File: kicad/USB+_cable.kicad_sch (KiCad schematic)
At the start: 5 parts, among them J1401 USB_C_Receptacle, J1402 USB_C_Receptacle

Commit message: Updated Digikey part numbers
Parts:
- J1402: Digikey WM12856CT-ND -> 664-12402072E512ACT-ND
- R1401: Digikey (none) -> P330JCT-ND; Purpose (none) -> LED current limiter
- R1402: Digikey (none) -> P1.0KJCT-ND; Purpose (none) -> LED current limiter
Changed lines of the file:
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@@
       (effects (font (size 1.524 1.524)) hide)
+    )
+    (property "Digikey" "P330JCT-ND" (id 4) (at 119.38 142.24 0)
+      (effects (font (size 1.27 1.27)) hide)
+    )
+    (property "Purpose" "LED current limiter" (id 5) (at 119.38 142.24 0)
+      (effects (font (size 1.27 1.27)) hide)
     )
     (pin "1")
@@
       (effects (font (size 1.27 1.27)) hide)
     )
-    (property "Digikey" "WM12856CT-ND" (id 5) (at 213.36 88.9 0)
+    (property "Digikey" "664-12402072E512ACT-ND" (id 5) (at 213.36 88.9 0)
       (effects (font (size 1.27 1.27)) hide)
     )
@@
       (effects (font (size 1.524 1.524)) hide)
     )
+    (property "Digikey" "P1.0KJCT-ND" (id 4) (at 134.62 142.24 0)
+      (effects (font (size 1.27 1.27)) hide)
+    )
+    (property "Purpose" "LED current limiter" (id 5) (at 134.62 142.24 0)
+      (effects (font (size 1.27 1.27)) hide)
+    )
     (pin "1")

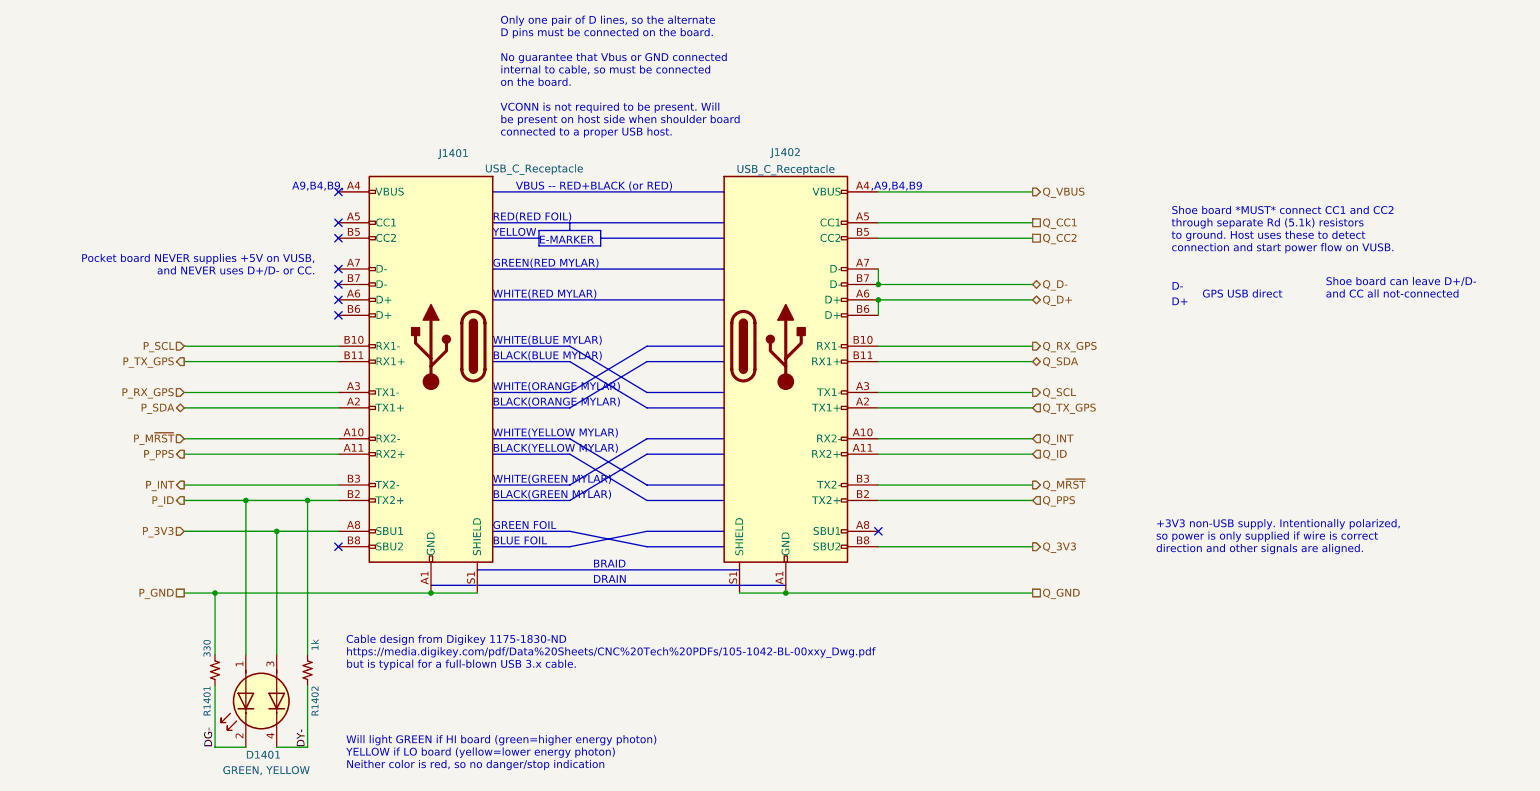
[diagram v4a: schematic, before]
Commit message: Added reference to USB cable on BOM
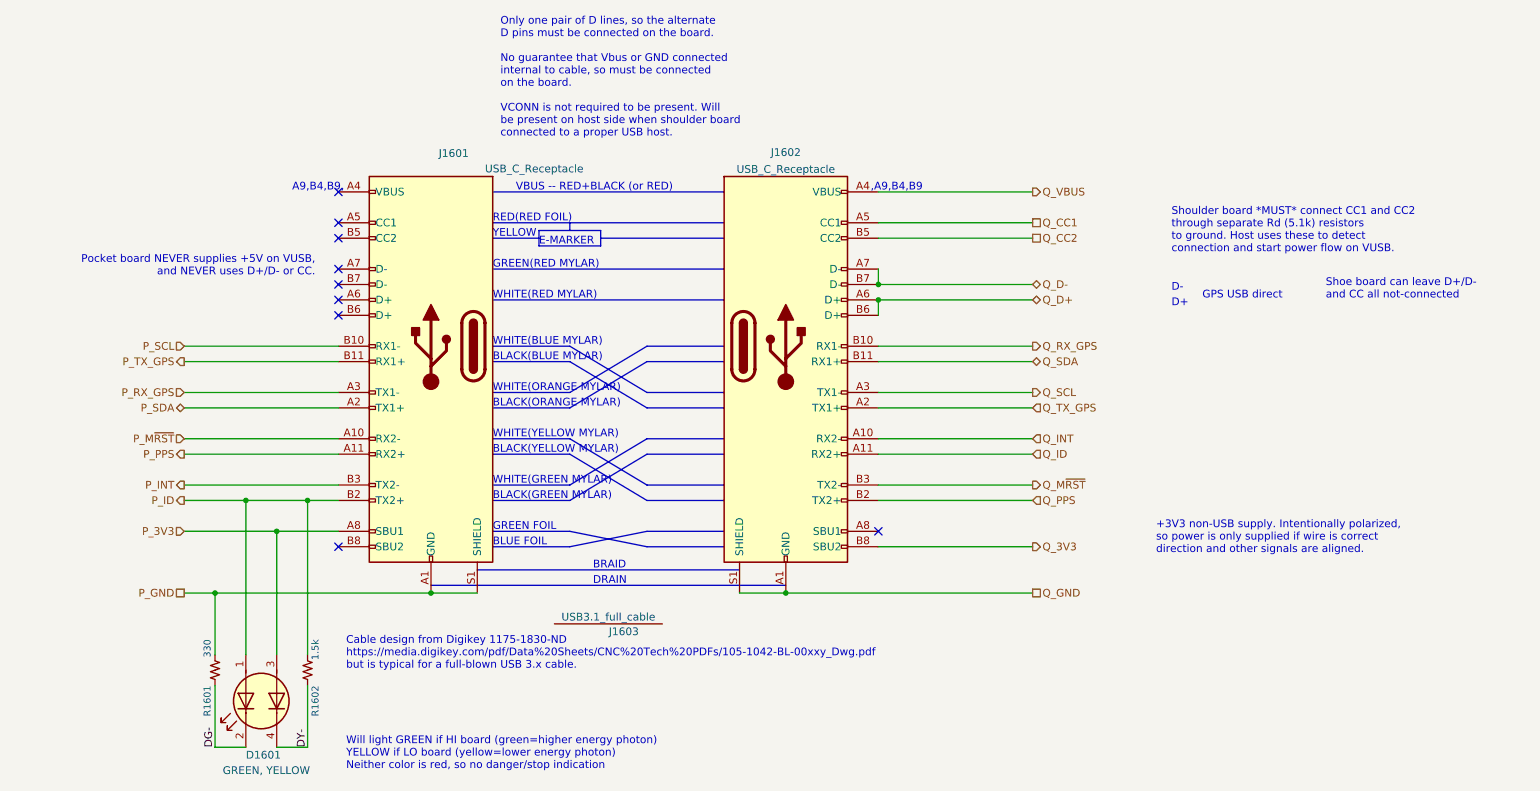
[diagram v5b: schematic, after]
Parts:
- added J1603: USB3.1_full_cable, symbol KwanSystems:USB3.1_full_cable
- R1602: renamed from R1402; value 1k -> 1.5k
- renumbered D1401 to D1601, J1401 to J1601, J1402 to J1602, R1401 to R1601
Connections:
- net at J1601.A4 (VBUS): now also J1601.A9 (VBUS), J1601.B4 (VBUS), J1601.B9 (VBUS)
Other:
- note added: "Shoulder board *MUST* connect CC1 and CC2 through separate Rd (5.1k) resistors to ground. Host uses these to detect connection and start power flow on VUSB."
- note removed: "Shoe board *MUST* connect CC1 and CC2 through separate Rd (5.1k) resistors to ground. Host uses these to detect connection and start power flow on VUSB."
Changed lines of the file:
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@@
     (effects (font (size 1.27 1.27)) (justify left bottom))
   )
-  (text "Shoe board *MUST* connect CC1 and CC2\nthrough separate Rd (5.1k) resistors \nto ground. Host uses these to detect\nconnection and start power flow on VUSB."
+  (text "Shoulder board *MUST* connect CC1 and CC2\nthrough separate Rd (5.1k) resistors \nto ground. Host uses these to detect\nconnection and start power flow on VUSB."
     (at 276.86 73.66 0)
     (effects (font (size 1.27 1.27)) (justify left bottom))
@@
     (effects (font (size 1.27 1.27)) (justify right))
   )
-  (symbol (lib_name "USB_C_Receptacle_1") (lib_id "Connector:USB_C_Receptacle") (at 154.94 88.9 0) (mirror y)
+  (symbol (lib_id "Connector:USB_C_Receptacle") (at 154.94 88.9 0) (mirror y)
     (in_bom yes) (on_board yes)
-    (property "Reference" "J1401" (id 0) (at 156.21 57.15 0)
+    (property "Reference" "J1601" (id 0) (at 156.21 57.15 0)
       (effects (font (size 1.27 1.27)) (justify right))
     )
@@
     )
     (property "Digikey" "664-12402072E512ACT-ND" (id 5) (at 154.94 88.9 0)
-      (effects (font (size 1.27 1.27)) hide)
-    )
-    (pin "A1")
-    (pin "A10")
-    (pin "A11")
-    (pin "A12")
-    (pin "A2")
-    (pin "A3")
-    (pin "A4")
-    (pin "A5")
-    (pin "A6")
-    (pin "A7")
-    (pin "A8")
-    (pin "B1")
-    (pin "B10")
-    (pin "B11")
-    (pin "B12")
-    (pin "B2")
-    (pin "B3")
-    (pin "B5")
-    (pin "B6")
-    (pin "B7")
-    (pin "B8")
-    (pin "S1")
-  )
-  (symbol (lib_id "Device:LED_Dual_AKAK") (at 127 147.32 90) (mirror x)
-    (in_bom yes) (on_board yes)
-    (property "Reference" "D1401" (id 0) (at 124.46 156.21 90)
-      (effects (font (size 1.27 1.27)) (justify right))
-    )
-    (property "Value" "GREEN, YELLOW" (id 1) (at 120.65 158.75 90)
-      (effects (font (size 1.27 1.27)) (justify right))
-    )
-    (property "Footprint" "KwanSystems:LEDKingbrightAPHB" (id 2) (at 127 148.082 0)
-      (effects (font (size 1.27 1.27)) hide)
-    )
-    (property "Datasheet" "~" (id 3) (at 127 148.082 0)
-      (effects (font (size 1.27 1.27)) hide)
-    )
-    (property "Digikey" "754-1956-1-ND" (id 4) (at 127 147.32 0)
-      (effects (font (size 1.27 1.27)) hide)
-    )
-    (property "Purpose" "Remote ID indicator" (id 5) (at 127 147.32 0)
-      (effects (font (size 1.27 1.27)) hide)
-    )
-    (pin "1")
-    (pin "2")
-    (pin "3")
-    (pin "4")
-  )
-  (symbol (lib_id "KwanSystems:RESISTOR") (at 119.38 142.24 90)
-    (in_bom yes) (on_board yes)
-    (property "Reference" "R1401" (id 0) (at 118.11 144.78 0)
-      (effects (font (size 1.143 1.143)) (justify right))
-    )
-    (property "Value" "330" (id 1) (at 118.11 137.16 0)
-      (effects (font (size 1.143 1.143)) (justify right))
-    )
-    (property "Footprint" "Resistor_SMD:R_0402_1005Metric" (id 2) (at 115.57 140.843 0)
-      (effects (font (size 0.508 0.508)) hide)
-    )
-    (property "Datasheet" "" (id 3) (at 127 131.445 0)
-      (effects (font (size 1.524 1.524)) hide)
-    )
-    (property "Digikey" "P330JCT-ND" (id 4) (at 119.38 142.24 0)
-      (effects (font (size 1.27 1.27)) hide)
-    )
-    (property "Purpose" "LED current limiter" (id 5) (at 119.38 142.24 0)
-      (effects (font (size 1.27 1.27)) hide)
-    )
-    (pin "1")
-    (pin "2")
-  )
-  (symbol (lib_id "Connector:USB_C_Receptacle") (at 213.36 88.9 0)
-    (in_bom yes) (on_board yes) (fields_autoplaced)
-    (property "Reference" "J1402" (id 0) (at 213.36 56.9935 0))
-    (property "Value" "USB_C_Receptacle" (id 1) (at 213.36 59.7686 0))
-    (property "Footprint" "KwanSystems:USB_C_Amphenol_MidMount" (id 2) (at 217.17 88.9 0)
-      (effects (font (size 1.27 1.27)) hide)
-    )
-    (property "Datasheet" "https://www.usb.org/sites/default/files/documents/usb_type-c.zip" (id 3) (at 217.17 88.9 0)
-      (effects (font (size 1.27 1.27)) hide)
-    )
-    (property "Purpose" "Remote board USB+ connector" (id 4) (at 213.36 88.9 0)
-      (effects (font (size 1.27 1.27)) hide)
-    )
-    (property "Digikey" "664-12402072E512ACT-ND" (id 5) (at 213.36 88.9 0)
       (effects (font (size 1.27 1.27)) hide)
     )
@@
     (pin "S1")
   )
+  (symbol (lib_id "Device:LED_Dual_AKAK") (at 127 147.32 90) (mirror x)
+    (in_bom yes) (on_board yes)
+    (property "Reference" "D1601" (id 0) (at 124.46 156.21 90)
+      (effects (font (size 1.27 1.27)) (justify right))
+    )
+    (property "Value" "GREEN, YELLOW" (id 1) (at 120.65 158.75 90)
+      (effects (font (size 1.27 1.27)) (justify right))
+    )
+    (property "Footprint" "KwanSystems:LEDKingbrightAPHB" (id 2) (at 127 148.082 0)
+      (effects (font (size 1.27 1.27)) hide)
+    )
+    (property "Datasheet" "~" (id 3) (at 127 148.082 0)
+      (effects (font (size 1.27 1.27)) hide)
+    )
+    (property "Digikey" "754-1956-1-ND" (id 4) (at 127 147.32 0)
+      (effects (font (size 1.27 1.27)) hide)
+    )
+    (property "Purpose" "Remote ID indicator" (id 5) (at 127 147.32 0)
+      (effects (font (size 1.27 1.27)) hide)
+    )
+    (pin "1")
+    (pin "2")
+    (pin "3")
+    (pin "4")
+  )
+  (symbol (lib_id "KwanSystems:RESISTOR") (at 119.38 142.24 90)
+    (in_bom yes) (on_board yes)
+    (property "Reference" "R1601" (id 0) (at 118.11 144.78 0)
+      (effects (font (size 1.143 1.143)) (justify right))
+    )
+    (property "Value" "330" (id 1) (at 118.11 137.16 0)
+      (effects (font (size 1.143 1.143)) (justify right))
+    )
+    (property "Footprint" "Resistor_SMD:R_0402_1005Metric" (id 2) (at 115.57 140.843 0)
+      (effects (font (size 0.508 0.508)) hide)
+    )
+    (property "Datasheet" "" (id 3) (at 127 131.445 0)
+      (effects (font (size 1.524 1.524)) hide)
+    )
+    (property "Digikey" "P330JCT-ND" (id 4) (at 119.38 142.24 0)
+      (effects (font (size 1.27 1.27)) hide)
+    )
+    (property "Purpose" "LED current limiter" (id 5) (at 119.38 142.24 0)
+      (effects (font (size 1.27 1.27)) hide)
+    )
+    (pin "1")
+    (pin "2")
+  )
+  (symbol (lib_id "Connector:USB_C_Receptacle") (at 213.36 88.9 0)
+    (in_bom yes) (on_board yes) (fields_autoplaced)
+    (property "Reference" "J1602" (id 0) (at 213.36 56.9935 0))
+    (property "Value" "USB_C_Receptacle" (id 1) (at 213.36 59.7686 0))
+    (property "Footprint" "KwanSystems:USB_C_Amphenol_MidMount" (id 2) (at 217.17 88.9 0)
+      (effects (font (size 1.27 1.27)) hide)
+    )
+    (property "Datasheet" "https://www.usb.org/sites/default/files/documents/usb_type-c.zip" (id 3) (at 217.17 88.9 0)
+      (effects (font (size 1.27 1.27)) hide)
+    )
+    (property "Purpose" "Remote board USB+ connector" (id 4) (at 213.36 88.9 0)
+      (effects (font (size 1.27 1.27)) hide)
+    )
+    (property "Digikey" "664-12402072E512ACT-ND" (id 5) (at 213.36 88.9 0)
+      (effects (font (size 1.27 1.27)) hide)
+    )
+    (pin "A1")
+    (pin "A10")
+    (pin "A11")
+    (pin "A12")
+    (pin "A2")
+    (pin "A3")
+    (pin "A4")
+    (pin "A5")
+    (pin "A6")
+    (pin "A7")
+    (pin "A8")
+    (pin "A9")
+    (pin "B1")
+    (pin "B10")
+    (pin "B11")
+    (pin "B12")
+    (pin "B2")
+    (pin "B3")
+    (pin "B4")
+    (pin "B5")
+    (pin "B6")
+    (pin "B7")
+    (pin "B8")
+    (pin "B9")
+    (pin "S1")
+  )
+  (symbol (lib_id "KwanSystems:USB3.1_full_cable") (at 184.15 133.35 0)
+    (in_bom yes) (on_board no)
+    (property "Reference" "J1603" (id 0) (at 186.69 135.89 0))
+    (property "Value" "USB3.1_full_cable" (id 1) (at 184.15 133.4794 0))
+    (property "Footprint" "" (id 2) (at 184.15 133.35 0)
+      (effects (font (size 1.27 1.27)) hide)
+    )
+    (property "Datasheet" "" (id 3) (at 184.15 133.35 0)
+      (effects (font (size 1.27 1.27)) hide)
+    )
+    (property "Digikey" "839-10-03674-ND" (id 4) (at 184.15 133.35 0)
+      (effects (font (size 1.27 1.27)) hide)
+    )
+    (property "Purpose" "Connector cables" (id 5) (at 184.15 133.35 0)
+      (effects (font (size 1.27 1.27)) hide)
+    )
+  )
   (symbol (lib_id "KwanSystems:RESISTOR") (at 134.62 142.24 90)
     (in_bom yes) (on_board yes)
-    (property "Reference" "R1402" (id 0) (at 135.89 144.78 0)
+    (property "Reference" "R1602" (id 0) (at 135.89 144.78 0)
       (effects (font (size 1.143 1.143)) (justify right))
     )
-    (property "Value" "1k" (id 1) (at 135.89 137.16 0)
+    (property "Value" "1.5k" (id 1) (at 135.89 137.16 0)
       (effects (font (size 1.143 1.143)) (justify right))
     )

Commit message: Added a NC to the board
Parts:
- renumbered D1601 to D1401, J1601 to J1401, J1602 to J1402, J1603 to J1403, R1601 to R1401, R1602 to R1402
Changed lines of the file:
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@@
   (symbol (lib_id "Connector:USB_C_Receptacle") (at 154.94 88.9 0) (mirror y)
     (in_bom yes) (on_board yes)
-    (property "Reference" "J1601" (id 0) (at 156.21 57.15 0)
+    (property "Reference" "J1401" (id 0) (at 156.21 57.15 0)
       (effects (font (size 1.27 1.27)) (justify right))
     )
@@
   (symbol (lib_id "Device:LED_Dual_AKAK") (at 127 147.32 90) (mirror x)
     (in_bom yes) (on_board yes)
-    (property "Reference" "D1601" (id 0) (at 124.46 156.21 90)
+    (property "Reference" "D1401" (id 0) (at 124.46 156.21 90)
       (effects (font (size 1.27 1.27)) (justify right))
     )
@@
   (symbol (lib_id "KwanSystems:RESISTOR") (at 119.38 142.24 90)
     (in_bom yes) (on_board yes)
-    (property "Reference" "R1601" (id 0) (at 118.11 144.78 0)
+    (property "Reference" "R1401" (id 0) (at 118.11 144.78 0)
       (effects (font (size 1.143 1.143)) (justify right))
     )
@@
   (symbol (lib_id "Connector:USB_C_Receptacle") (at 213.36 88.9 0)
     (in_bom yes) (on_board yes) (fields_autoplaced)
-    (property "Reference" "J1602" (id 0) (at 213.36 56.9935 0))
+    (property "Reference" "J1402" (id 0) (at 213.36 56.9935 0))
     (property "Value" "USB_C_Receptacle" (id 1) (at 213.36 59.7686 0))
     (property "Footprint" "KwanSystems:USB_C_Amphenol_MidMount" (id 2) (at 217.17 88.9 0)
@@
   (symbol (lib_id "KwanSystems:USB3.1_full_cable") (at 184.15 133.35 0)
     (in_bom yes) (on_board no)
-    (property "Reference" "J1603" (id 0) (at 186.69 135.89 0))
+    (property "Reference" "J1403" (id 0) (at 186.69 135.89 0))
     (property "Value" "USB3.1_full_cable" (id 1) (at 184.15 133.4794 0))
     (property "Footprint" "" (id 2) (at 184.15 133.35 0)
@@
   (symbol (lib_id "KwanSystems:RESISTOR") (at 134.62 142.24 90)
     (in_bom yes) (on_board yes)
-    (property "Reference" "R1602" (id 0) (at 135.89 144.78 0)
+    (property "Reference" "R1402" (id 0) (at 135.89 144.78 0)
       (effects (font (size 1.143 1.143)) (justify right))
     )
